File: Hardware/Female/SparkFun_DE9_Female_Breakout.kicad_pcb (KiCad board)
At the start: 2 copper layers, 22.9 x 31.8 mm, 43 parts, among them J1 DE9-Female, J2 Conn_01x09, J3 Conn_01x01, J4 Conn_01x01

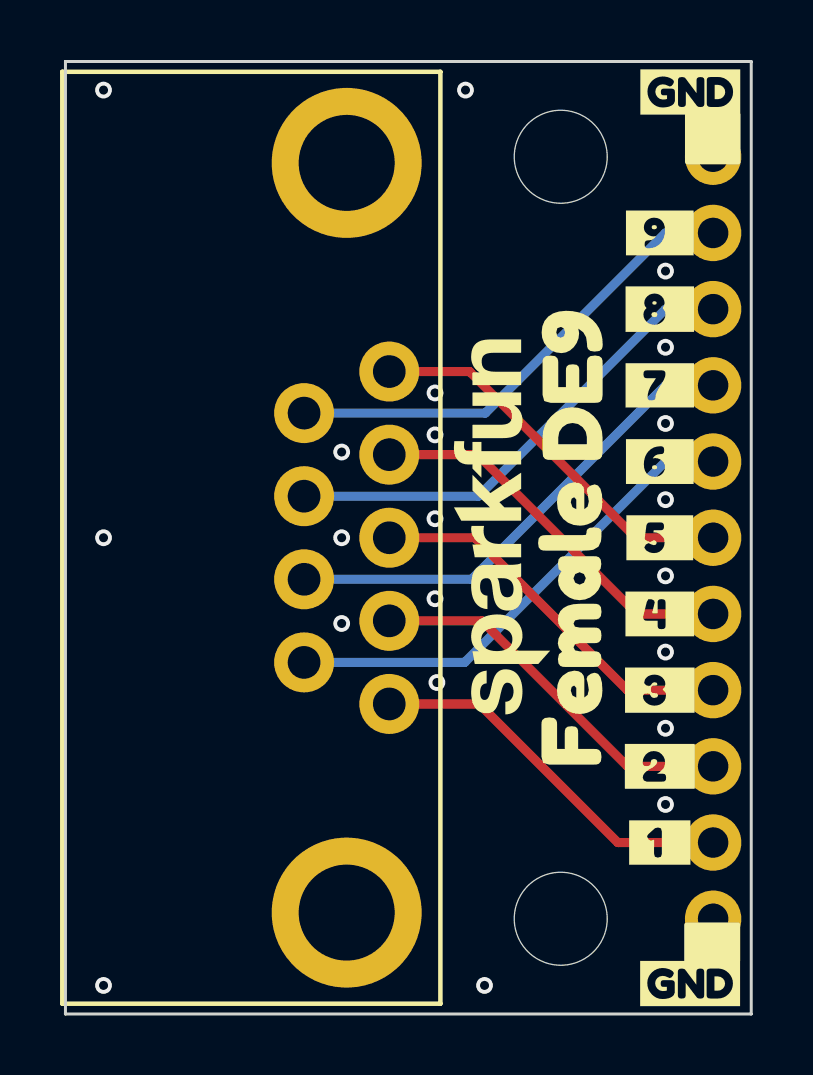
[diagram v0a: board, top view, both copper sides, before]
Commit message: Removes the local symbols/footprints, moves designs to Hardware folder
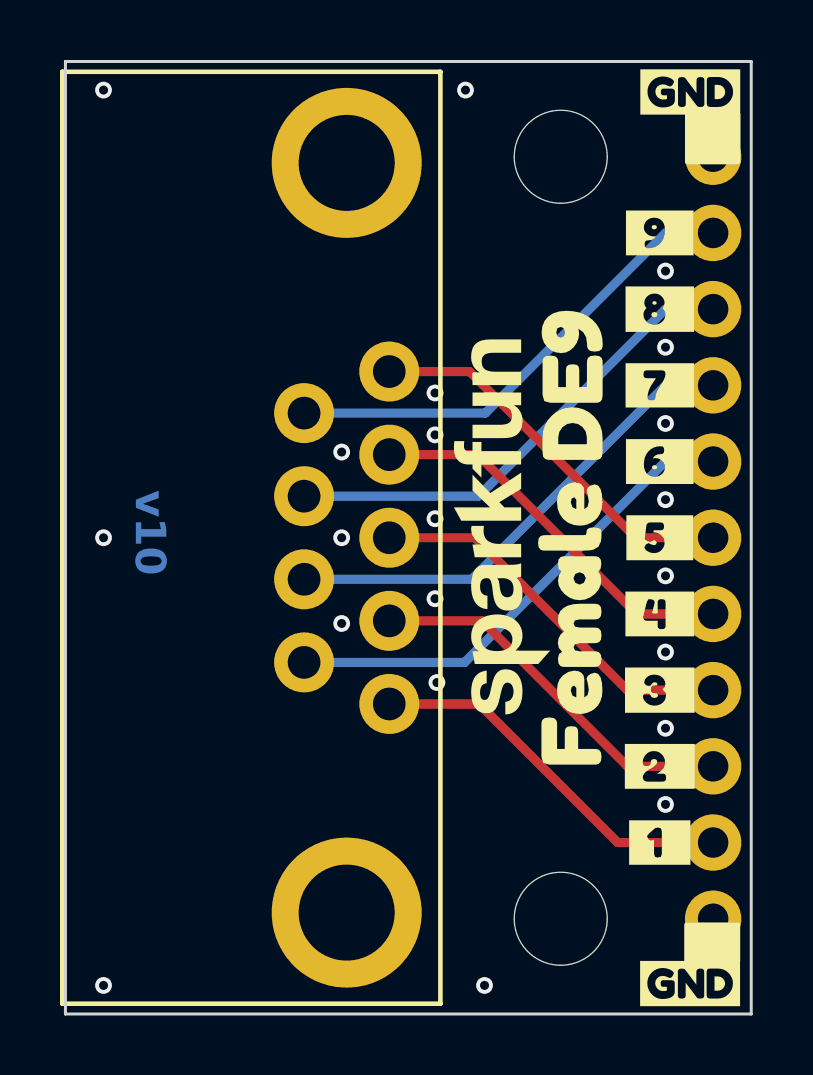
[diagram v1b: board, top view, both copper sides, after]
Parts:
- J1: value DE9-Female -> DE9 Female; footprint DE9-Footprints:DE9_Female -> SparkFun-Connector:DE9_Female
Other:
- board text added: "v10"
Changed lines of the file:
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@@
 		(embedded_fonts no)
 	)
-	(footprint "DE9-Footprints:DE9_Female"
+	(footprint "SparkFun-Connector:DE9_Female"
 		(layer "F.Cu")
 		(at 120.269 108.585 90)
-		(tags "A-DS 09 A/KG-T4S ")
 		(property "Reference" "J1"
-			(at 0 -6.5 90)
+			(at 0 -0.5 90)
 			(unlocked yes)
 			(layer "F.Fab")
+			(hide yes)
 			(effects
 				(font
-					(size 0.5 0.5)
-					(thickness 0.1)
-					(bold yes)
+					(size 1 1)
+					(thickness 0.15)
 				)
 			)
 		)
-		(property "Value" "DE9-Female"
-			(at 0 -5.5 90)
+		(property "Value" "DE9 Female"
+			(at 0 -5.8 90)
 			(unlocked yes)
 			(layer "F.Fab")
@@
 		)
 		(property "Datasheet" "https://www.lcsc.com/datasheet/lcsc_datasheet_2411220417_XUNPU-D-SUB-DR-9PCM-CB_C19077337.pdf"
-			(at 0 -10.919998 90)
+			(at 0 0 90)
+			(unlocked yes)
 			(layer "F.Fab")
 			(hide yes)
 			(effects
 				(font
-					(size 1.27 1.27)
+					(size 1 1)
 					(thickness 0.15)
 				)
@@
 		)
 		(property "Description" ""
-			(at 0 -10.919998 90)
+			(at 0 0 90)
+			(unlocked yes)
 			(layer "F.Fab")
 			(hide yes)
 			(effects
 				(font
-					(size 1.27 1.27)
+					(size 1 1)
 					(thickness 0.15)
 				)
 			)
 		)
-		(property ki_fp_filters "CONN_A-DF 09 A/KG-T4S_ASM")
 		(sheetname "/")
 		(sheetfile "SparkFun_DE9_Female_Breakout.kicad_sch")
-		(attr through_hole)
+		(attr smd)
 		(fp_line
 			(start 15.5321 -10.9)
 			(end -15.5321 -10.9)
 			(stroke
-				(width 0.15)
+				(width 0.1524)
 				(type solid)
 			)
@@
 			(end -15.5321 1.703802)
 			(stroke
-				(width 0.15)
+				(width 0.1524)
 				(type solid)
 			)
@@
 			(end 15.5321 -10.9)
 			(stroke
-				(width 0.15)
+				(width 0.1524)
 				(type solid)
 			)
@@
 			(end 15.5321 1.703802)
 			(stroke
-				(width 0.15)
+				(width 0.1524)
 				(type solid)
 			)
@@
 			(layer "F.Fab")
 		)
+		(fp_text user "${REFERENCE}"
+			(at 0 -4.519998 90)
+			(unlocked yes)
+			(layer "F.Fab")
+			(effects
+				(font
+					(size 0.5 0.5)
+					(thickness 0.1)
+					(bold yes)
+				)
+			)
+		)
 		(pad "1" thru_hole circle
 			(at -5.539999 0 90)
@@
 		)
 		(pad "3" thru_hole circle
-			(at 0 0 90)
+			(at 0 0 180)
 			(size 2 2)
 			(drill 1.09)
@@
 		)
 		(pad "5" thru_hole circle
-			(at 5.539999 0 90)
+			(at 5.539999 0 180)
 			(size 2 2)
 			(drill 1.09)
@@
 		)
 		(embedded_fonts no)
-		(model "/home/amo/SparkFun/SparkFun_DB9_Breakout/DB9_Footprint/DB9-Female.step"
+		(model "${SPARKFUN_KICAD_LIBRARY}/Footprints/SparkFun-3D-models/Connector/DE9-Female.step"
 			(offset
-				(xyz 0 12.669998 1)
+				(xyz 0 12.5 0)
 			)
 			(scale
@@
 				(font
 					(size 0.001 0.001)
+					(thickness 0.15)
 				)
 				(justify mirror)
@@
 				(font
 					(size 0.001 0.001)
+					(thickness 0.15)
 				)
 				(justify mirror)
@@
 		(layer "Edge.Cuts")
 	)
+	(gr_text "v10"
+		(at 111.6965 106.9975 270)
+		(layer "B.Cu" knockout)
+		(effects
+			(font
+				(size 1.016 1.016)
+				(thickness 0.254)
+				(bold yes)
+			)
+			(justify left bottom)
+		)
+	)
 	(gr_text "Inner Copper Weight: 0.5oz"
